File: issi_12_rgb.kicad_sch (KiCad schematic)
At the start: 26 parts, among them Q1 3412, Q10 3412, Q11 3412, Q12 3412, Q13 3412, Q14 3412, Q15 3412, Q16 3412, Q2 3412, Q3 3412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

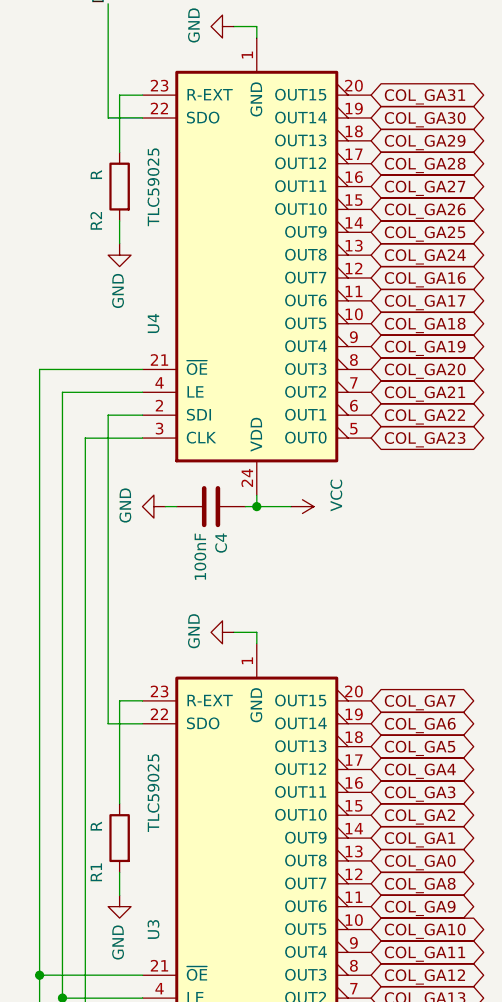
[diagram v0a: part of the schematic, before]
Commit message: add BOM
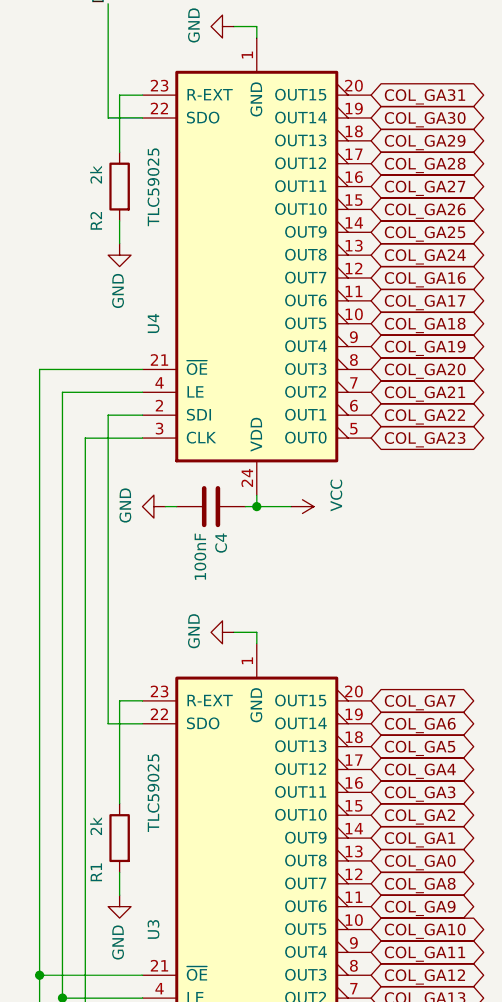
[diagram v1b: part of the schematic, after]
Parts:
- C1, C2, C3, C4: Mfg (none) -> Samsung Electro-Mechanics; PN (none) -> CL10B104KB8NNNC
- Q1, Q10, Q11, Q12, Q13, Q14, Q15, Q16, Q2, Q3, Q4, Q5, Q6, Q7, Q8, Q9: Mfg (none) -> LRC; PN (none) -> LP0404N3T5G
- R1, R2: value R -> 2k; Mfg (none) -> UNI-ROYAL(Uniroyal Elec); PN (none) -> 0603WAF2001T5E
- U1, U2: Mfg (none) -> Nexperia; PN (none) -> 74HC595PW\,118
- U3, U4: Mfg (none) -> Texas Instruments; PN (none) -> TLC59282DBQR
